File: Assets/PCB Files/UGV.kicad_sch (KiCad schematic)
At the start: 77 parts, among them J13 USB3_A, J15 Screw_Terminal_01x12, J16 Screw_Terminal_01x12, J17 Screw_Terminal_01x12, J18 Screw_Terminal_01x12, Q1 AO3400A, U2 LMR33630ADDA, U3 SN74LVC8T245, U4 Teensy4.1, U5 SN74LVC8T245

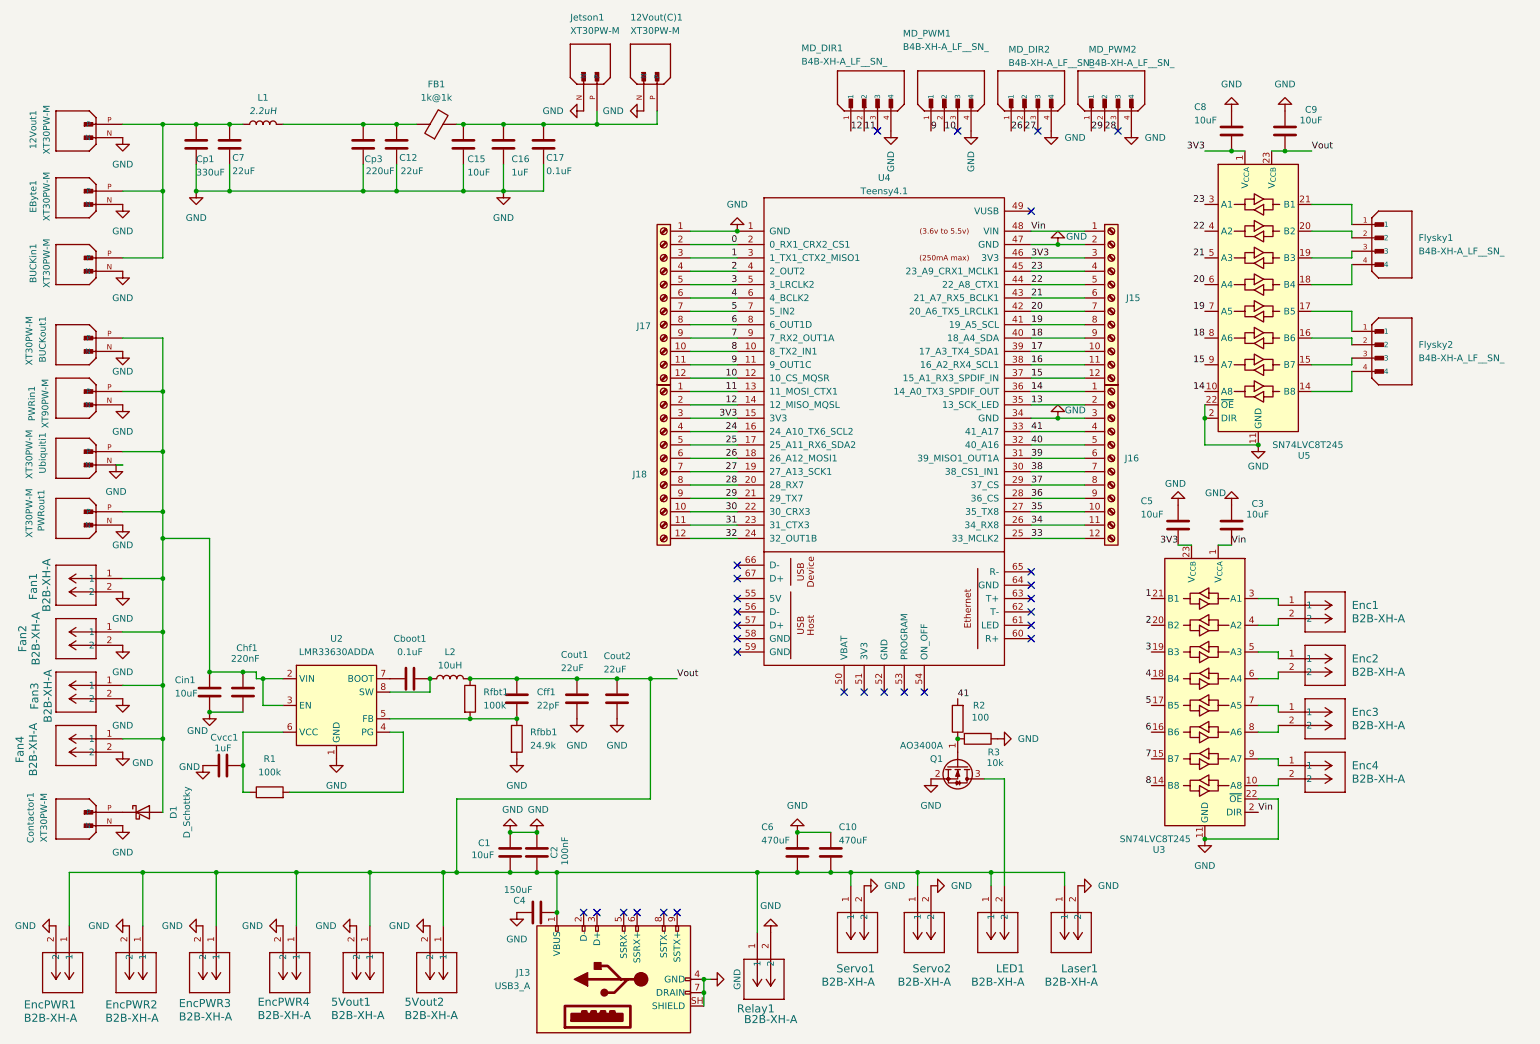
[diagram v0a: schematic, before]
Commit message: Changed the footprint
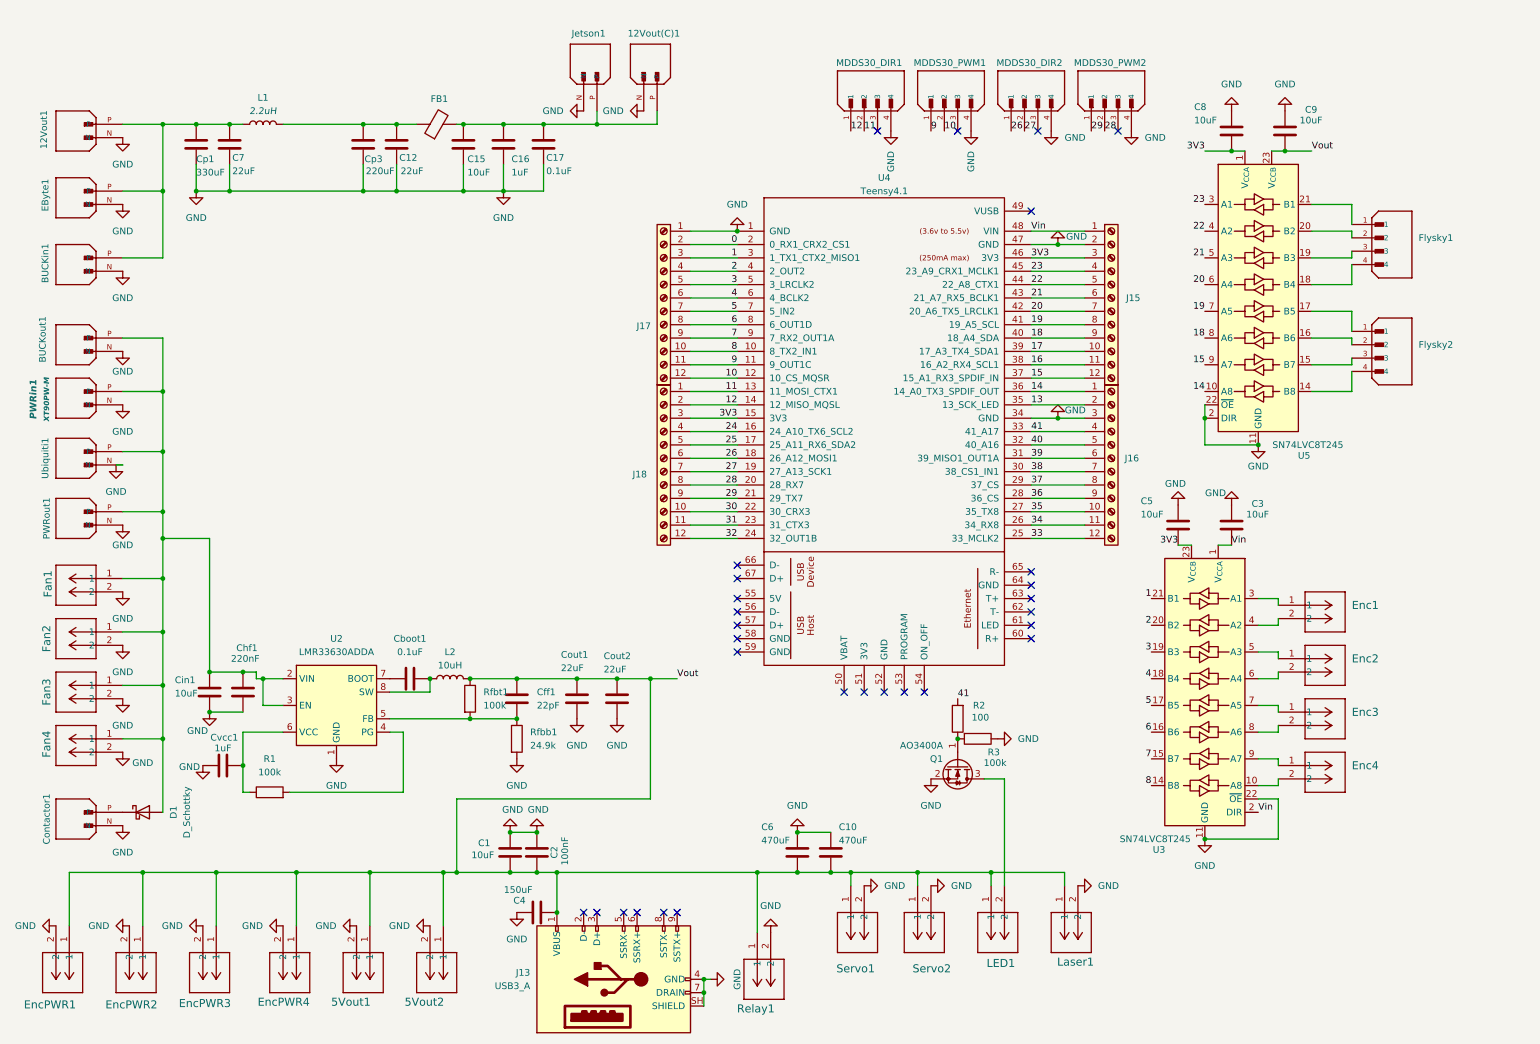
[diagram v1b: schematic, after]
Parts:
- 12Vout(C)1, 12Vout1, BUCKin1, BUCKout1, Contactor1, EByte1, Jetson1, PWRout1, Ubiquiti1: footprint XT30PW-M (1):AMASS_XT30PW-M -> UGV_Custom:AMASS_XT30PW-M; MP XT30PW-M -> (none); MPN (none) -> XT30PW-M
- 5Vout1, 5Vout2, EncPWR1, EncPWR2, EncPWR3, EncPWR4, LED1, Laser1, Relay1, Servo1, Servo2: MPN (none) -> B2B-XH-A
- C1, C15, C3, C5, C8, C9, Cin1: footprint Capacitor_SMD:C_1210_3225Metric -> Capacitor_SMD:C_1210_3225Metric_Pad1.33x2.70mm_HandSolder
- C12, C7: footprint Capacitor_SMD:C_1210_3225Metric -> Capacitor_SMD:C_1210_3225Metric_Pad1.33x2.70mm_HandSolder; MPN (none) -> C1210C226K3RACTU
- C16, C17, C2, Cboot1, Cvcc1: footprint Capacitor_SMD:C_0603_1608Metric -> Capacitor_SMD:C_1206_3216Metric_Pad1.33x1.80mm_HandSolder
- Cff1: footprint Capacitor_SMD:C_0603_1608Metric -> Capacitor_SMD:C_0805_2012Metric_Pad1.18x1.45mm_HandSolder
- Chf1: footprint Capacitor_SMD:C_1206_3216Metric -> Capacitor_SMD:C_1206_3216Metric_Pad1.33x1.80mm_HandSolder
- Cout1: MPN (none) -> C1210C226K3RACTU
- Cout2: footprint Capacitor_SMD:C_0603_1608Metric_Pad1.08x0.95mm_HandSolder -> Capacitor_SMD:C_1210_3225Metric_Pad1.33x2.70mm_HandSolder; MPN (none) -> C1210C226K3RACTU
- Enc1, Enc2, Enc3, Enc4: value B2B-XH-A -> B2B-XH-A-BK; MPN (none) -> B2B-XH-A-BK
- FB1: footprint BLM21PG220SN1D:BEADC2012X105N -> Inductor_SMD:L_0805_2012Metric_Pad1.05x1.20mm_HandSolder
- Fan1, Fan2, Fan3, Fan4: value B2B-XH-A -> B2B-XH-A-R; MPN (none) -> B2B-XH-A-R
- Flysky1, Flysky2: footprint B4B-XH-A_LF__SN_:JST_B4B-XH-A_LF__SN_ -> Connector_JST:JST_XH_B4B-XH-A_1x04_P2.50mm_Vertical; MP B4B-XH-A (LF)(SN) -> (none); MPN (none) -> B4B-XH-A (LF)(SN)
- J13: footprint EasyEDA_Lib:USB-3.0-TH_U233-091N-4BLPC17-11 -> UGV_Custom:USB-3.0-TH_U233-091N-4BLPC17-11
- L2: footprint Inductor_SMD:L_Vishay_IHLP-2525 -> UGV_Custom:SRR1280-101M
- MDDS30_DIR1: renamed from MD_DIR1; footprint B4B-XH-A_LF__SN_:JST_B4B-XH-A_LF__SN_ -> Connector_JST:JST_XH_B4B-XH-A_1x04_P2.50mm_Vertical; MP B4B-XH-A (LF)(SN) -> (none); MPN (none) -> B4B-XH-A (LF)(SN)
- MDDS30_DIR2: renamed from MD_DIR2; footprint B4B-XH-A_LF__SN_:JST_B4B-XH-A_LF__SN_ -> Connector_JST:JST_XH_B4B-XH-A_1x04_P2.50mm_Vertical
- MDDS30_PWM1: renamed from MD_PWM1; footprint B4B-XH-A_LF__SN_:JST_B4B-XH-A_LF__SN_ -> Connector_JST:JST_XH_B4B-XH-A_1x04_P2.50mm_Vertical; MP B4B-XH-A (LF)(SN) -> (none); MPN (none) -> B4B-XH-A (LF)(SN)
- MDDS30_PWM2: renamed from MD_PWM2; footprint B4B-XH-A_LF__SN_:JST_B4B-XH-A_LF__SN_ -> Connector_JST:JST_XH_B4B-XH-A_1x04_P2.50mm_Vertical; MP B4B-XH-A (LF)(SN) -> (none); MPN (none) -> B4B-XH-A (LF)(SN)
- PWRin1: footprint XT90PW-M:AMASS_XT90PW-M -> Connector_AMASS:AMASS_XT90PW-M_1x02_P10.90mm_Horizontal
- R1, Rfbb1, Rfbt1: footprint Resistor_SMD:R_0402_1005Metric -> Resistor_SMD:R_1206_3216Metric_Pad1.30x1.75mm_HandSolder
- R2: footprint Resistor_SMD:R_0402_1005Metric -> Resistor_SMD:R_0805_2012Metric_Pad1.20x1.40mm_HandSolder
- R3: value 10k -> 100k; footprint Resistor_SMD:R_0402_1005Metric -> Resistor_SMD:R_1206_3216Metric_Pad1.30x1.75mm_HandSolder
- U2: footprint LMR33630ADDA:VREG_LM5017MR_NOPB -> UGV_Custom:LMR33630ADDAR
- U3, U5: footprint SN74LVC8T245DWR:SOIC127P1030X265-24N -> Package_SO:SOIC-24W_7.5x15.4mm_P1.27mm
- U4: footprint teensy.pretty-master:Teensy41 -> UGV_Custom:Teensy41
